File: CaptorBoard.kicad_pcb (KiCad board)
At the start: 2 copper layers, 90 x 50 mm, 56 parts, among them J2 Screw_Terminal_01x03, J3 Screw_Terminal_01x03, J5 Conn_01x04, J7 Conn_01x08, K1 G5LE-1-DC5, K2 G5LE-1-DC5, Q1 2N7002E, Q2 2N7002E, SW1 SW_PUSH, SW2 SW_PUSH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

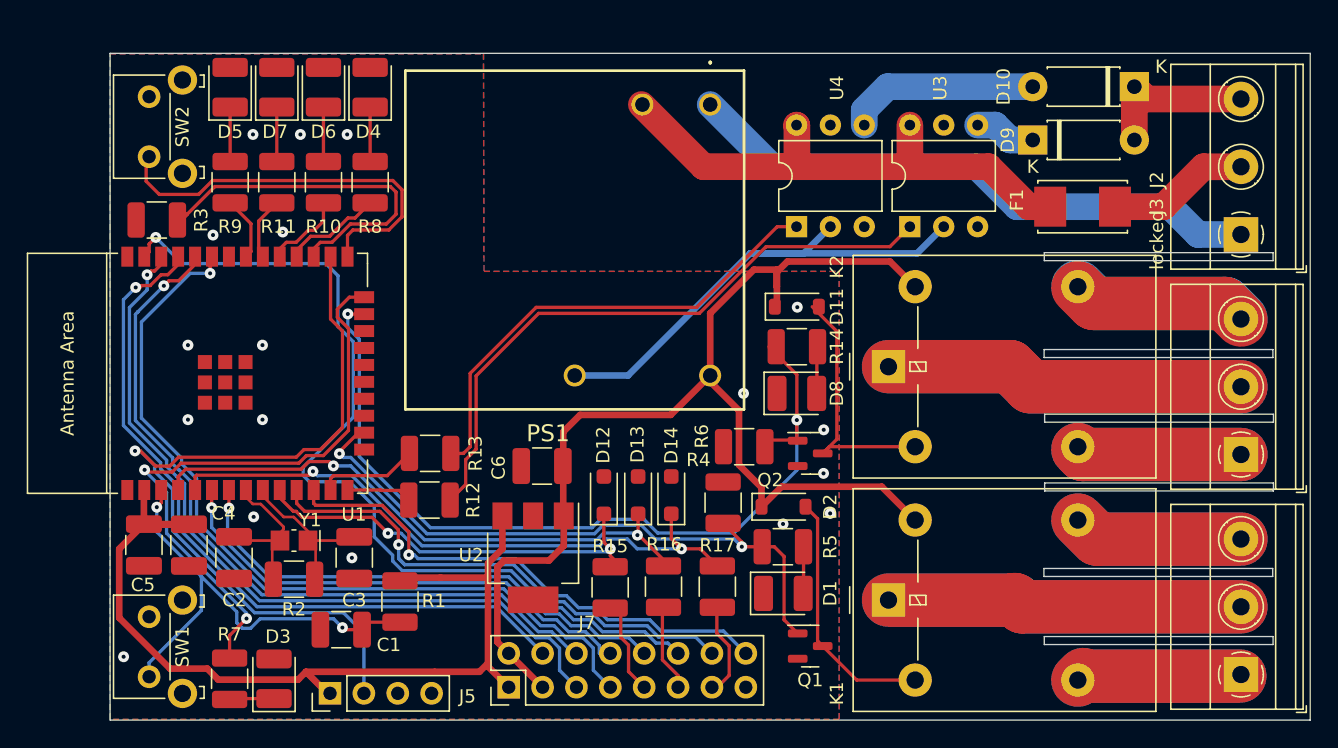
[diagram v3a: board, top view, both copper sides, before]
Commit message: add CEM protection, and change reférance for Digikey distributor
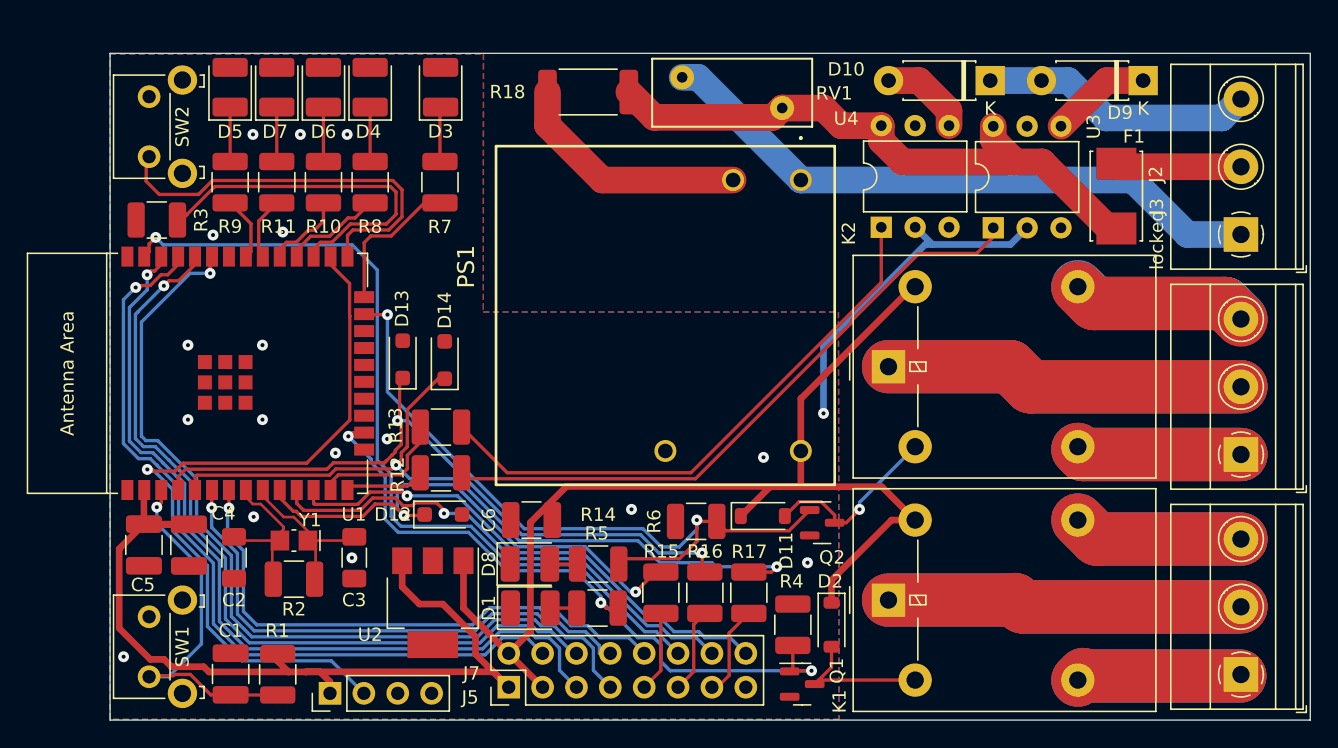
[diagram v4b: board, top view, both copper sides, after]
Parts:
- added R18: 12, Resistor_SMD:R_2512_6332Metric_Pad1.40x3.35mm_HandSolder, F.Cu at (130.8, 52.9)
- added RV1: B72210S0351K101, Varistor:RV_Disc_D12mm_W5.1mm_P7.5mm, F.Cu at (145.4, 54.1)
- C2, C3: footprint Capacitor_SMD:C_1210_3225Metric_Pad1.33x2.70mm_HandSolder -> Capacitor_SMD:C_1206_3216Metric_Pad1.33x1.80mm_HandSolder
- PS1: value PSK-5D-5 -> LD03-23B05R2
- U1: value ESP32-WROOM-32E-N4 -> ESP32-WROOM-32E-H4
- moved D3 46.1 mm to (119.8, 52.5)
- moved R7 40.4 mm to (119.7, 59.7), turned to -90 degrees
- moved D8 23.8 mm to (126.5, 88.3)
- moved R14 22.1 mm to (131.6, 88.3), turned to 180 degrees
- moved D13 20.4 mm to (116.9, 72.9)
- moved D14 19.8 mm to (120.1, 73.0)
- moved D1 19.0 mm to (126.5, 91.6)
- moved D11 15.9 mm to (143.9, 84.7)
- moved R5 14.6 mm to (131.6, 91.6), turned to 180 degrees
- moved D12 12.1 mm to (120.0, 84.6), turned to 0 degrees
- moved D10 10.8 mm to (161.0, 52.0)
- moved R1 10.7 mm to (107.6, 96.6)
- moved R4 10.5 mm to (146.2, 92.8)
- moved D2 9.55 mm to (149.1, 92.8), turned to -90 degrees
- moved D9 9.40 mm to (172.5, 52.0), turned to 180 degrees
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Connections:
- PS1 pad 2: /Phase -> /Phase_f
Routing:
- net /POWER: track 46.3 -> 11.0 mm, vias 2 -> 0
- net /Phase_f: track 0.00 -> 18.1 mm
- net GND: track 39.5 -> 25.9 mm
- net /ANA2: track 46.7 -> 58.7 mm
- net /REL2: track 65.0 -> 54.6 mm
- net /ANA1: track 43.6 -> 52.5 mm
- net /CMD2: track 12.4 -> 20.6 mm
- net Net-(D2-A): track 19.0 -> 11.0 mm
- net /P2: track 14.5 -> 6.59 mm
- net /ANA0: track 31.6 -> 39.0 mm
- net Net-(R13-Pad1): track 36.2 -> 42.9 mm
- net /RESET: track 35.1 -> 28.4 mm, vias 2 -> 1
- net Net-(D11-A): track 19.3 -> 13.9 mm, vias 0 -> 1
- net /GPIO23: track 68.9 -> 64.1 mm
- net /SDA_EXT: track 61.8 -> 66.1 mm
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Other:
- outline, holes or cut-outs redrawn

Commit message: change a bad foot print for fuse
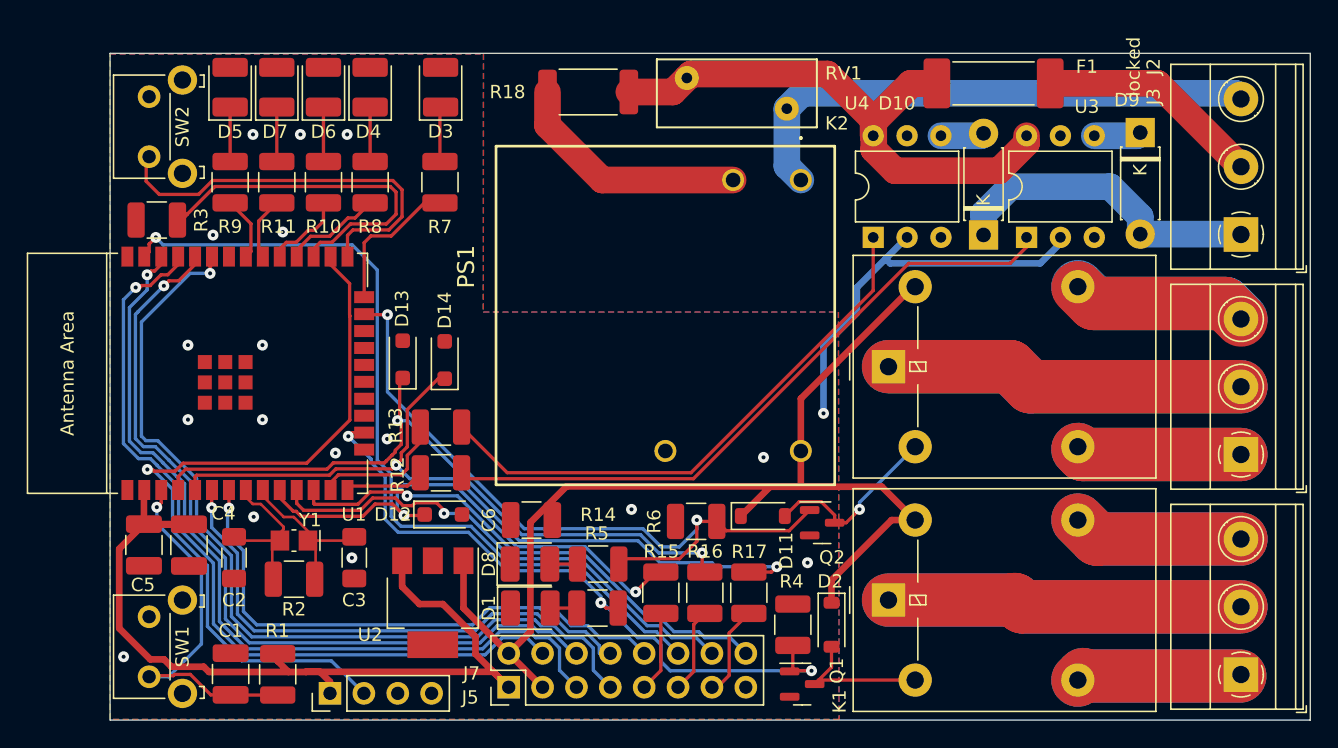
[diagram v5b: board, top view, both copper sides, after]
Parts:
- F1: footprint Fuse:Fuseholder_Littelfuse_Nano2_157x -> Fuse:Fuse_Schurter_UMT250
- moved F1 12.5 mm to (161.2, 52.2), turned to 0 degrees
- moved D10 11.6 mm to (160.5, 63.6), turned to 90 degrees
- moved RV1 7.50 mm to (138.2, 51.9), turned to 0 degrees
- moved D9 3.90 mm to (172.2, 55.9), turned to -90 degrees
- moved U3 2.60 mm to (163.7, 63.8)
- moved U4 0.97 mm to (152.2, 63.8)
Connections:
- J2 pad 1: /Neutre -> /CMD2
- J2 pad 3: /CMD2 -> /Neutre
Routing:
- net /Phase_in: track 9.44 -> 16.9 mm
- net /Neutre: track 46.8 -> 40.5 mm
- net /Phase: track 45.3 -> 50.1 mm
- net GND: track 25.9 -> 30.2 mm
- net /P1: track 7.57 -> 3.54 mm
- net /CMD2: track 20.6 -> 24.0 mm
- net /P2: track 6.59 -> 3.27 mm
- net Net-(R12-Pad1): track 48.3 -> 50.5 mm
- net Net-(R13-Pad1): track 42.9 -> 41.9 mm

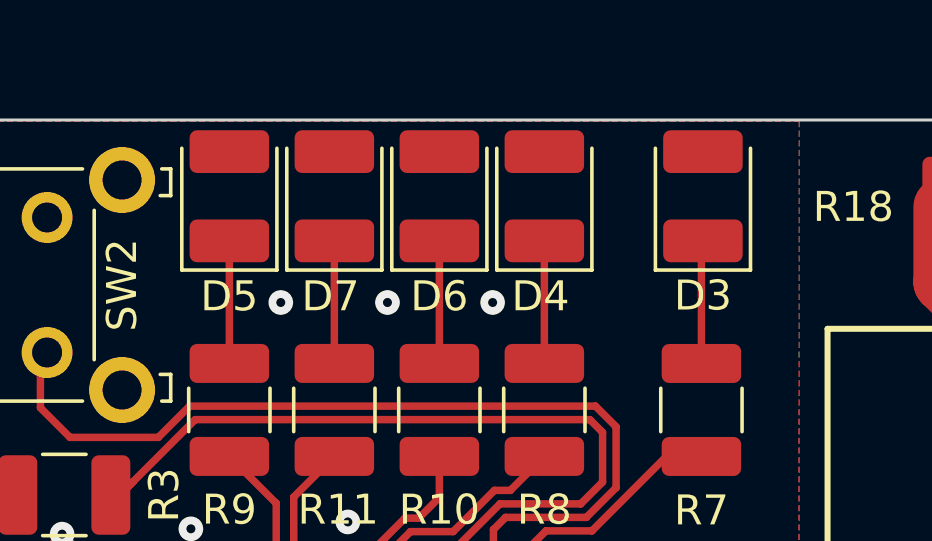
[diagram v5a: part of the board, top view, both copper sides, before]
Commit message: LED it inversed
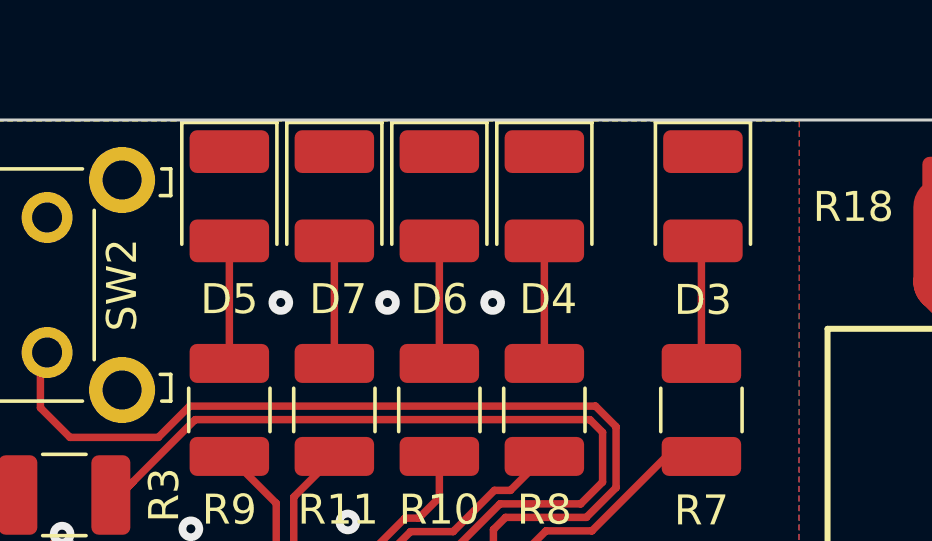
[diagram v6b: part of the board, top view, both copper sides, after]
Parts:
- turned D3 to -90 degrees
- turned D4 to -90 degrees
- turned D5 to -90 degrees
- turned D6 to -90 degrees
- turned D7 to -90 degrees
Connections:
- D3 pad 1: Net-(D3-K) -> GND
- D3 pad 2: GND -> Net-(D3-A)
- D4 pad 1: Net-(D4-K) -> GND
- D4 pad 2: GND -> Net-(D4-A)
- D5 pad 1: Net-(D5-K) -> GND
- D5 pad 2: GND -> Net-(D5-A)
- D6 pad 1: Net-(D6-K) -> GND
- D6 pad 2: GND -> Net-(D6-A)
- D7 pad 1: Net-(D7-K) -> GND
- D7 pad 2: GND -> Net-(D7-A)
- R10 pad 1: Net-(D6-K) -> Net-(D6-A)
- R11 pad 1: Net-(D7-K) -> Net-(D7-A)
- R7 pad 1: Net-(D3-K) -> Net-(D3-A)
- R8 pad 1: Net-(D4-K) -> Net-(D4-A)
- R9 pad 1: Net-(D5-K) -> Net-(D5-A)
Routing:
- net Net-(D3-K): track 4.11 -> 0.00 mm
- net Net-(D3-A): track 0.00 -> 4.11 mm
- net Net-(D7-K): track 4.08 -> 0.00 mm
- net Net-(D7-A): track 0.00 -> 4.08 mm
- net Net-(D6-K): track 4.08 -> 0.00 mm
- net Net-(D6-A): track 0.00 -> 4.08 mm
- net Net-(D5-K): track 4.08 -> 0.00 mm
- net Net-(D5-A): track 0.00 -> 4.08 mm
- net Net-(D4-K): track 3.50 -> 0.00 mm
- net Net-(D4-A): track 0.00 -> 3.50 mm

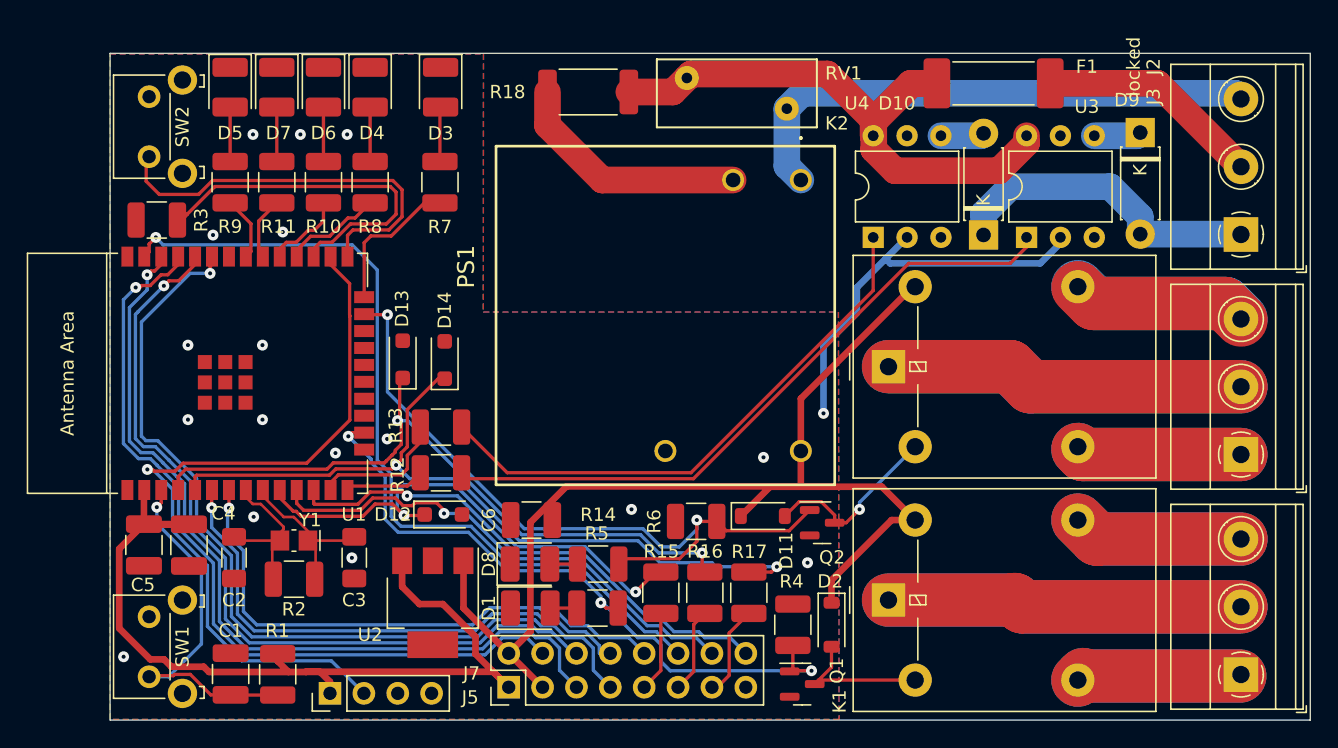
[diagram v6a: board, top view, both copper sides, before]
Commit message: route AN0 channel
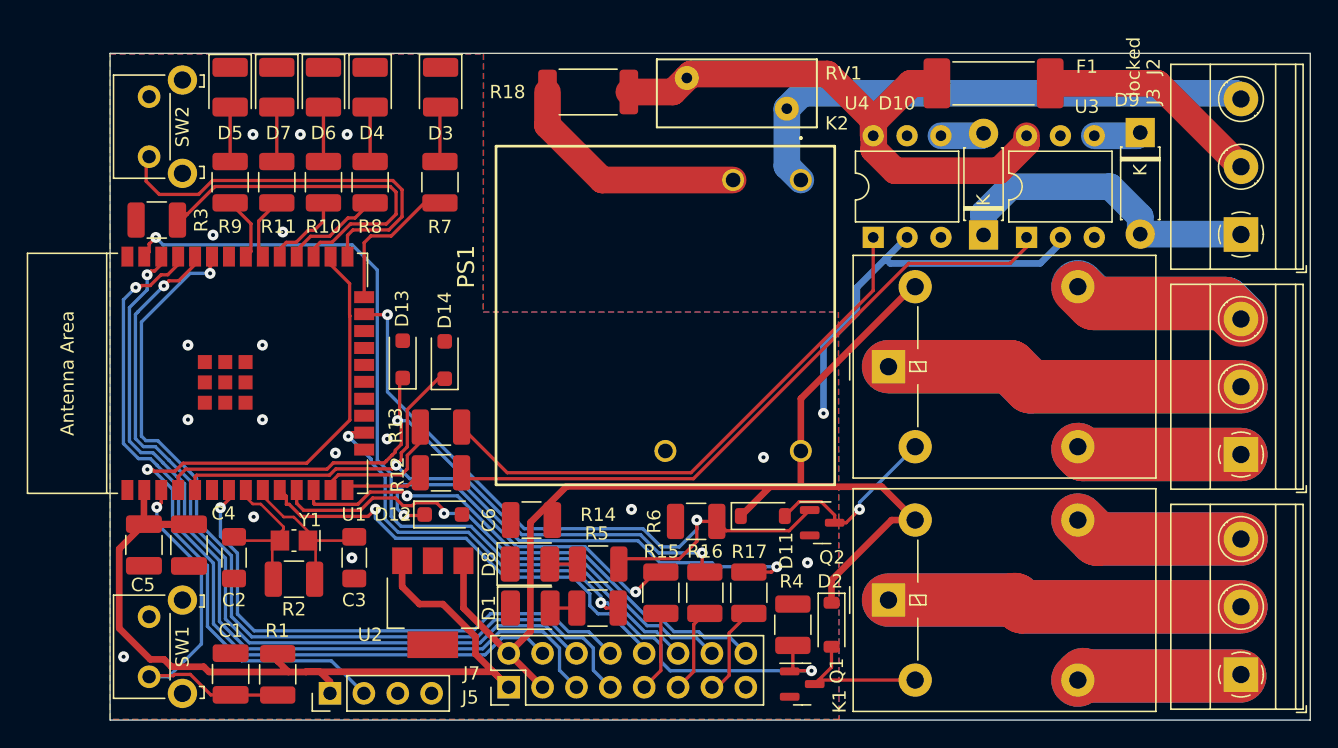
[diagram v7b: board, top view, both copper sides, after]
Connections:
- J7 pad 10: /GPIO35 -> /GPIO25
- J7 pad 8: /GPIO34 -> /GPIO35
- U1 pad 10: /ANA0 -> /GPIO25
- U1 pad 6: /GPIO34 -> /ANA0
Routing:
- net /GPIO34: track 40.7 -> 0.00 mm, vias 1 -> 0
- net /GPIO25: track 0.00 -> 34.3 mm, vias 0 -> 1
- net /ANA0: track 38.6 -> 26.9 mm
- net /GPIO35: track 42.1 -> 40.3 mm
- net /PILOT_2: track 10.3 -> 8.58 mm
- net /POWER: track 11.0 -> 9.84 mm
- net /XN: track 11.9 -> 10.7 mm
- net /XP: track 11.6 -> 10.5 mm
- net Net-(U1-GPIO16): track 27.5 -> 26.6 mm
- net /RX: track 61.3 -> 60.4 mm
- net Net-(R12-Pad1): track 50.5 -> 49.8 mm
- net /ANA1: track 52.5 -> 51.9 mm
- net /CAPTOR: track 57.4 -> 56.8 mm
- net /SCL_EXT: track 62.7 -> 62.1 mm
- net /TX: track 60.1 -> 59.5 mm
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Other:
- board text added: "5V - 2 TX - 4 RX - 6 GPIO35 - 8 GPIO25 - 10 GPIO23 - 12 GPIO26 - 14 GPIO27 - 16"
- board text removed: "5V - 2 TX - 4 RX - 6 GPIO34 - 8 GPIO35 - 10 GPIO23 - 12 GPIO26 - 14 GPIO27 - 16"

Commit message: Migrate to Kicad 8.0
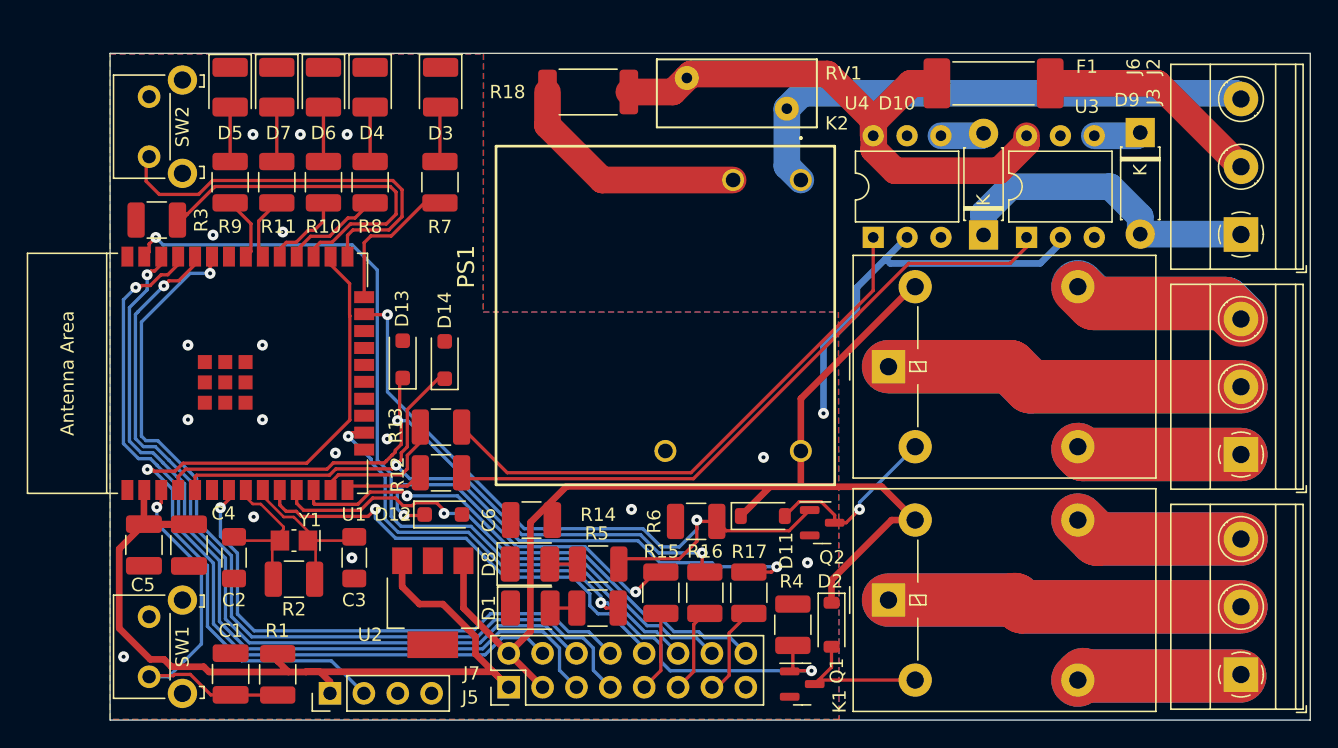
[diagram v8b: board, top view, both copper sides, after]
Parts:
- renumbered locked to J6
